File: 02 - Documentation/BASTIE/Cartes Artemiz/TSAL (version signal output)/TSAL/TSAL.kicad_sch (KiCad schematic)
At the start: 127 parts, among them J1 2P Droit 2-11-2022, J2 2P Droit 2-11-2022, J3 2P Droit 2-11-2022, J4 3P Droit 22-11-2032, J6 2P Droit 2-11-2022, J7 4P Droit 22-11-2042, J8 3P Droit 22-11-2032, J9 2P Droit 2-11-2022, Q1 PMOS SI2343CDS-T1-GE3, Q2 PMOS SI2343CDS-T1-GE3, U1 Opamp_Quad, U2 Opamp

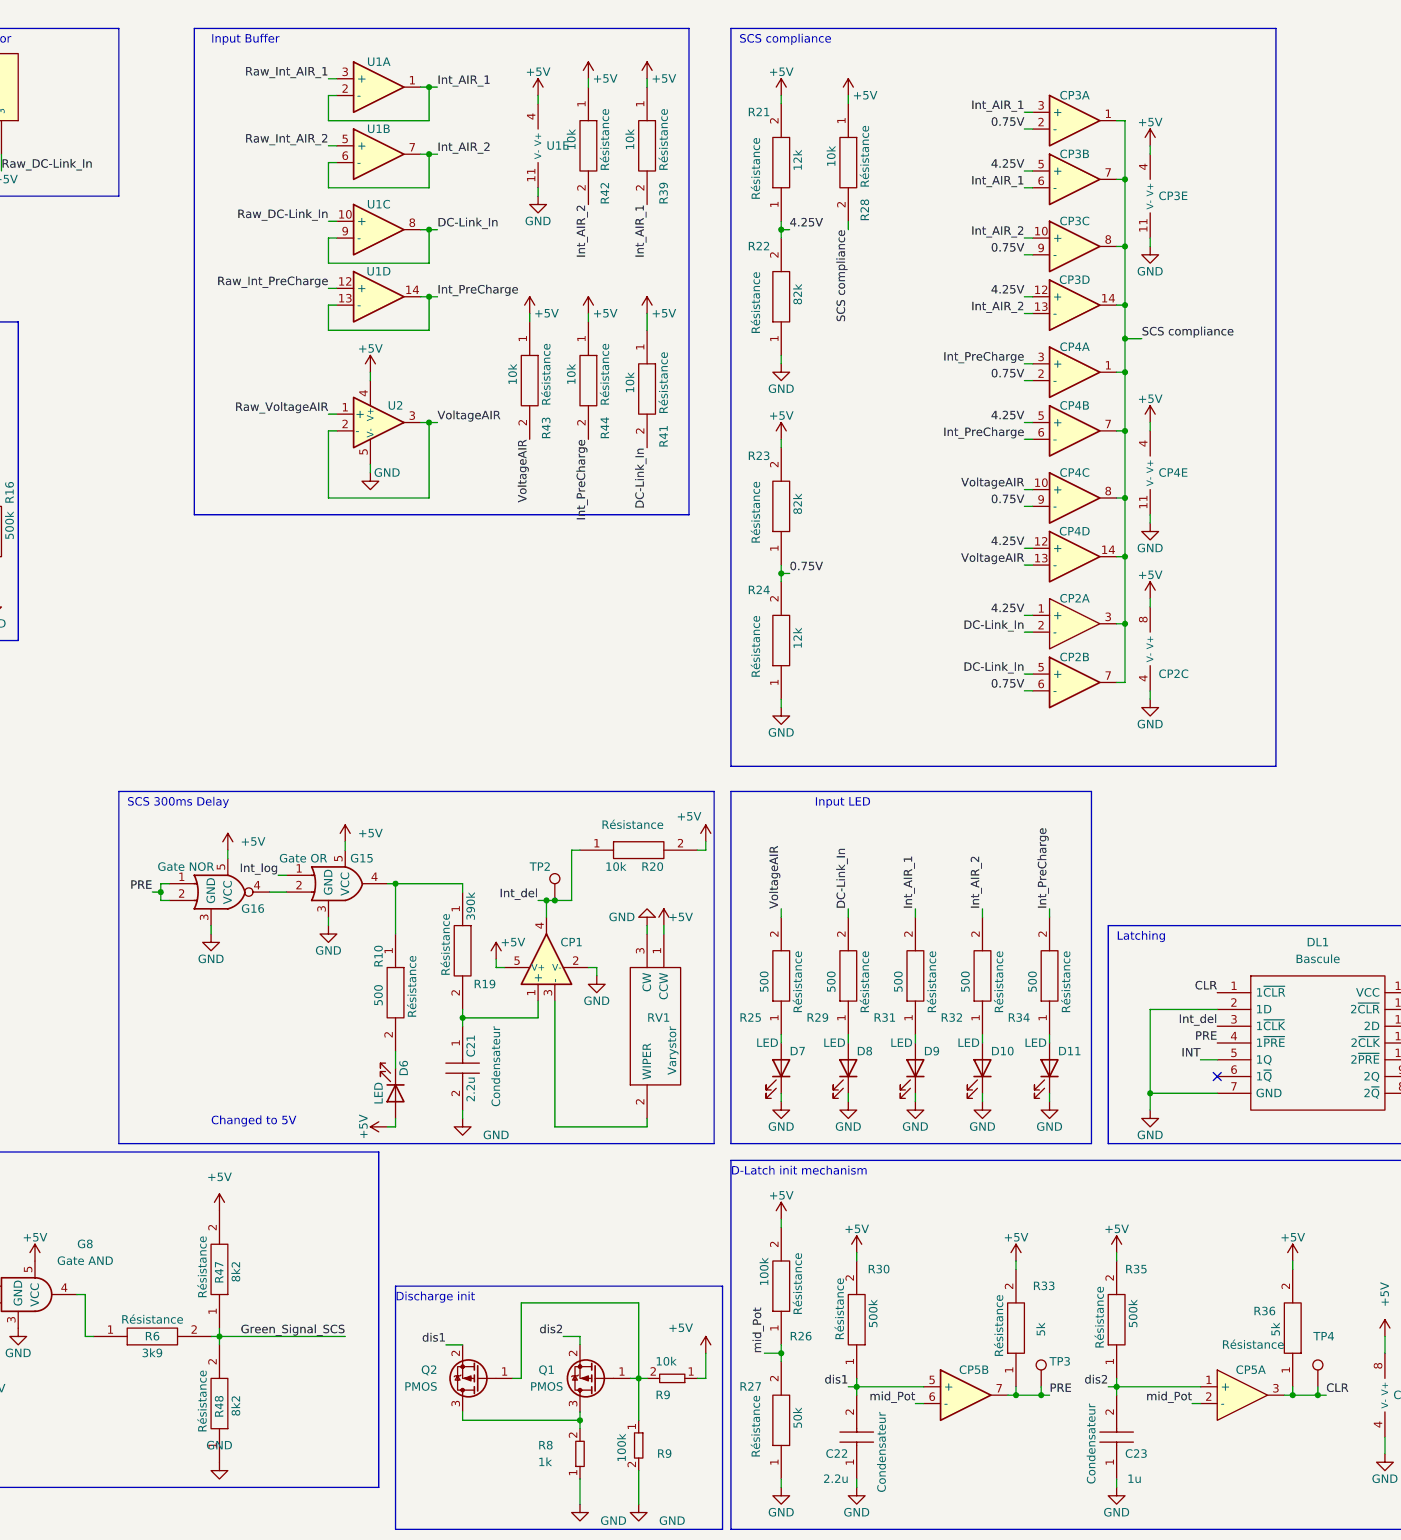
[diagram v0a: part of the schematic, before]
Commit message: Modifications cartes
Prise en compte des retours ECT + PCBs
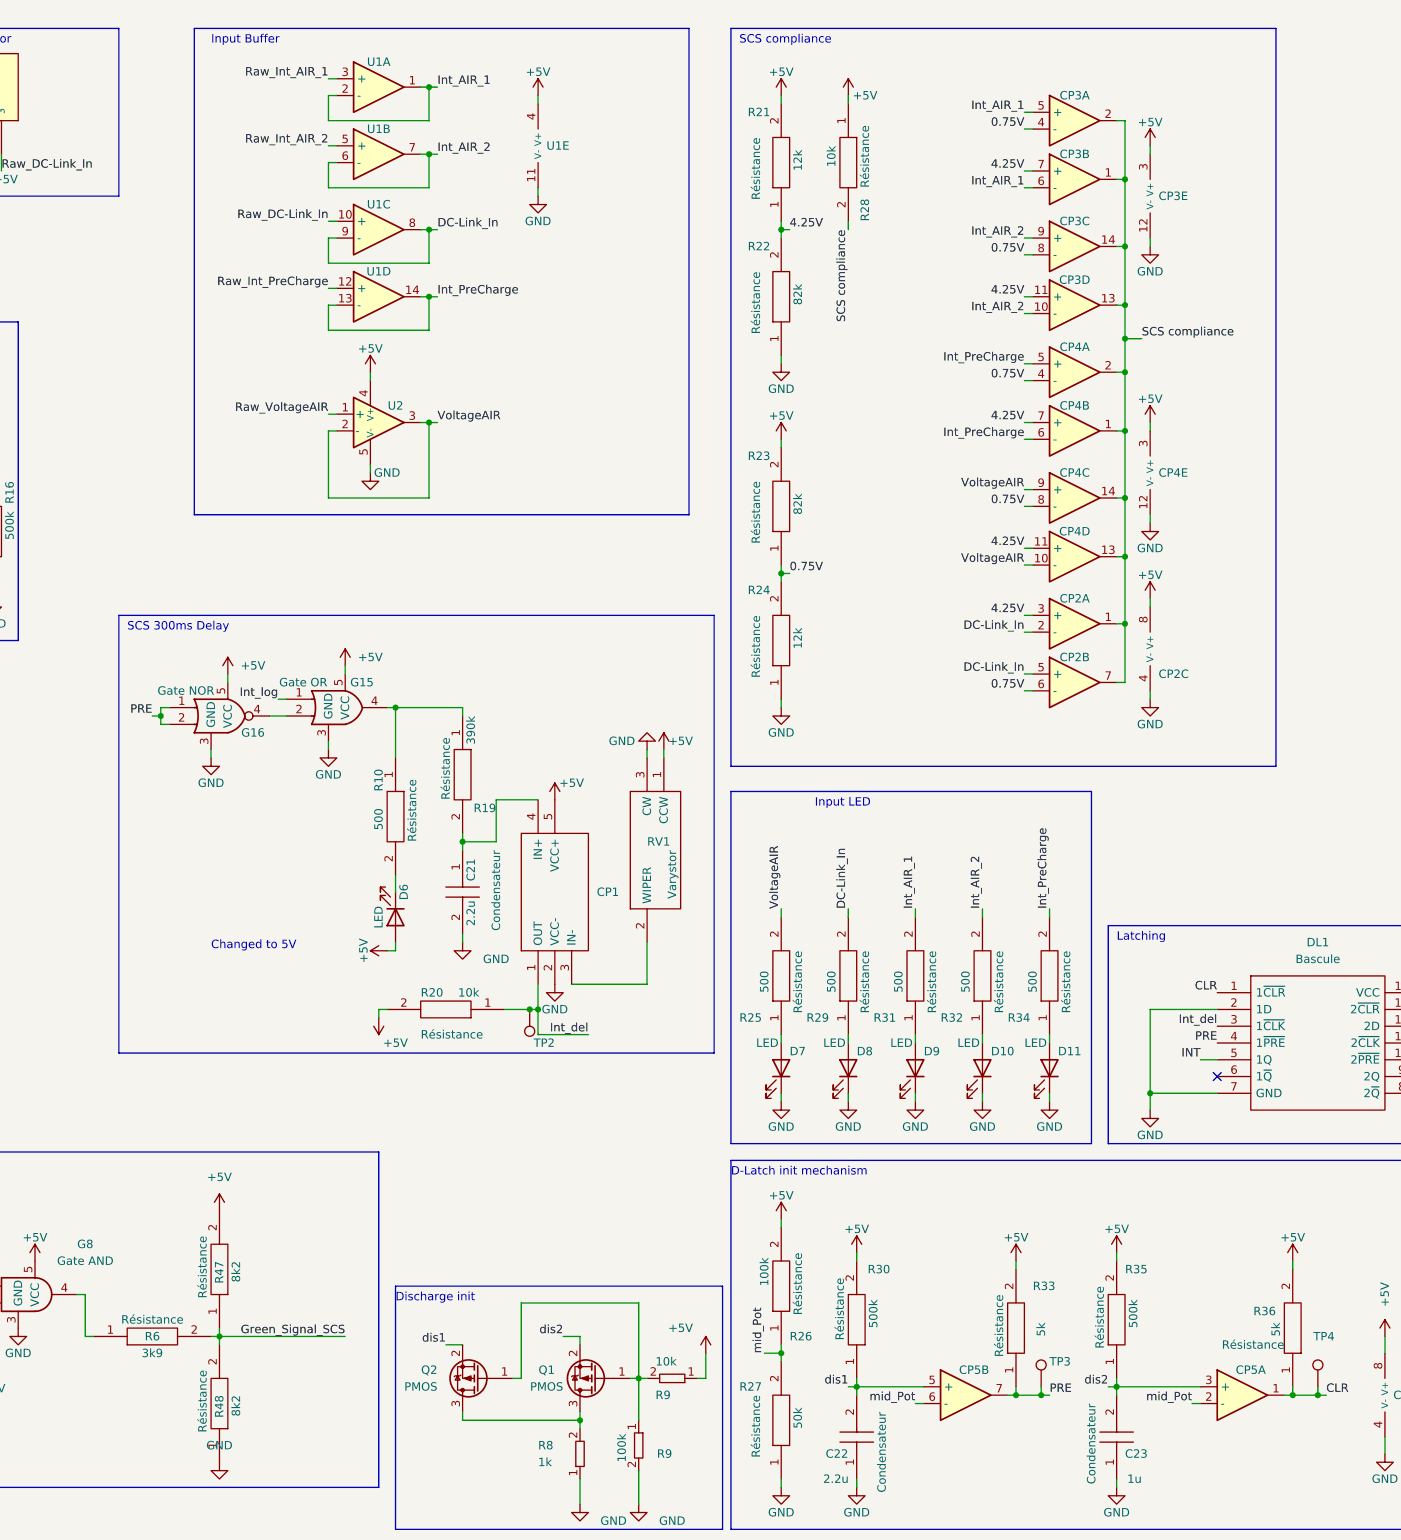
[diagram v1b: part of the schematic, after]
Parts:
- removed CP1: Comparator, Package_TO_SOT_SMD:SOT-353_SC-70-5, symbol Basic_SPICE:Comparator
- removed R39, R41, R42, R43, R44: 10k, EPSA:RESC3216X70N, symbol EPSA_lib:Résistance RK73H2BLTDD2152F
- added CP1: Comparateur TS391ILT, EPSA_lib:SOT95P280X145-5N, symbol EPSA_lib:Dep_Comparateur TS391ILT
- CP2, CP5: symbol EPSA_Lib:Opamp_Dual -> EPSA_lib:Comparator_Dual; Manufacturer_Part_Number TLV9062QPWRQ1 -> LMV393IPWR; Mouser Part Number 595-TLV9062QPWRQ1 -> 595-LMV393IPWR
- CP3, CP4: symbol EPSA_Lib:Opamp_Quad -> EPSA_lib:Comparator_Quad; Manufacturer_Part_Number TLV9064QPWRQ1 -> LMV339IPWR; Mouser Part Number 595-TLV9064QPWRQ1 -> 595-LMV339IPWR
- U2: symbol EPSA_Lib:Opamp -> EPSA_lib:Opamp
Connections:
- net +5V: now also CP3.3 (V+), CP4.3 (V+), CP1.5 (VCC+); no longer CP3.4 (V+), CP4.4 (V+)
- net 0.75V: now also CP3.4 (-), CP3.8 (-), CP4.4 (-), CP4.8 (-); no longer CP3.2 (-), CP3.9 (-), CP4.2 (-), CP4.9 (-)
- net 4.25V: now also CP2.3 (+), CP3.11 (+), CP3.7 (+), CP4.11 (+), CP4.7 (+); no longer CP2.1 (+), CP3.12 (+), CP3.5 (+), CP4.12 (+), CP4.5 (+)
- net CLR: now also CP5.1; no longer CP5.3
- net GND: now also CP3.12 (V-), CP4.12 (V-), CP1.2 (VCC-); no longer CP3.11 (V-), CP4.11 (V-)
- net Int_AIR_1: now also CP3.5 (+); no longer CP3.3 (+)
- net Int_AIR_2: now also CP3.10 (-), CP3.9 (+); no longer CP3.10 (+), CP3.13 (-)
- net Int_PreCharge: now also CP4.5 (+); no longer CP4.3 (+)
- net Int_del: now also CP1.1 (OUT)
- net SCS compliance: now also CP2.1, CP3.1, CP3.13, CP3.14, CP3.2, CP4.1, CP4.13, CP4.14, CP4.2; no longer CP2.3, CP3.1, CP3.14, CP3.7, CP3.8, CP4.1, CP4.14, CP4.7, CP4.8
- net VoltageAIR: now also CP4.10 (-), CP4.9 (+); no longer CP4.10 (+), CP4.13 (-)
- net dis2: now also CP5.3 (+); no longer CP5.1 (+)
- net at C21.1, R19.2: now also CP1.4 (IN+)
- net at RV1.2 (WIPER): now also CP1.3 (IN-)
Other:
- moved on the sheet: C21, D6, G15, G16, R10, R19, R20, RV1, TP2
